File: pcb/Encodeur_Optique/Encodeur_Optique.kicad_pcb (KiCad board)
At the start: 2 copper layers, 20 x 28.5 mm, 10 parts, among them J1 Conn_01x04, U1 GP1A52LRJ00F, U2 74LVC1G17

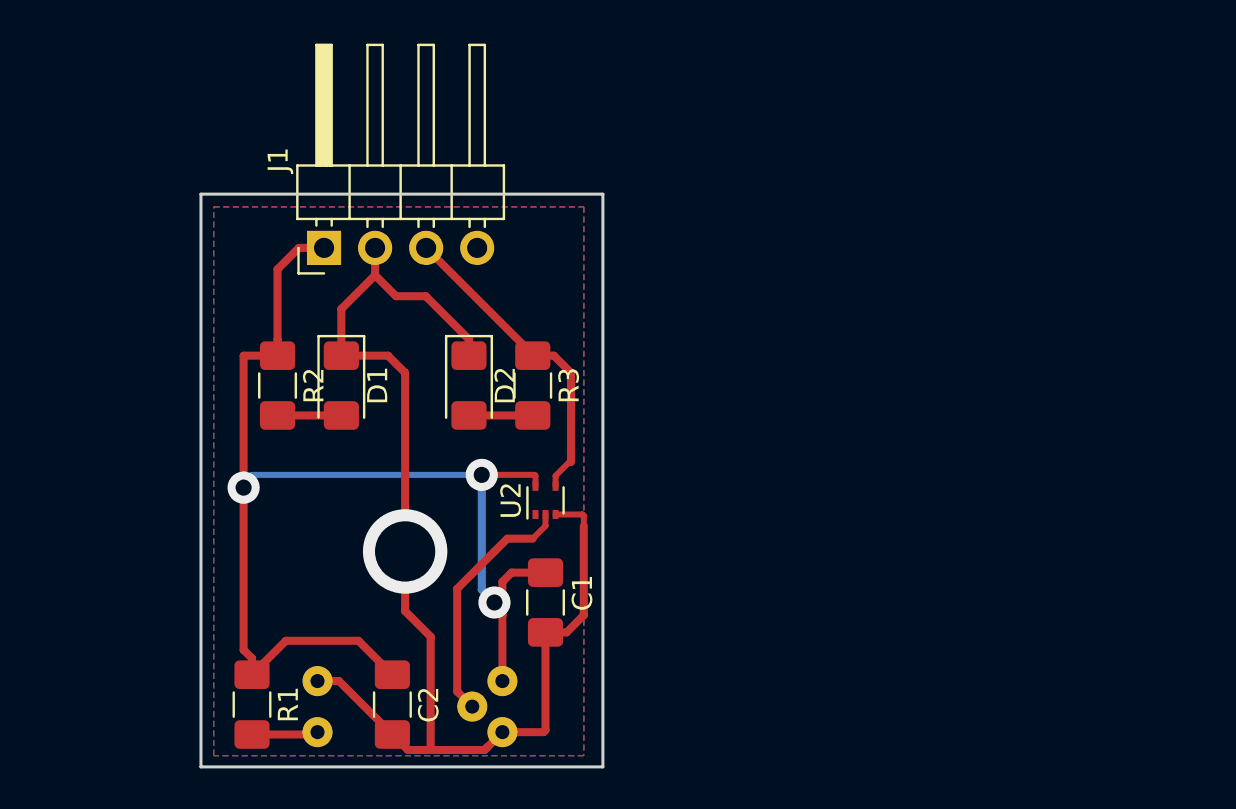
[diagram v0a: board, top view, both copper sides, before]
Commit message: Encoder OK, Camera OK
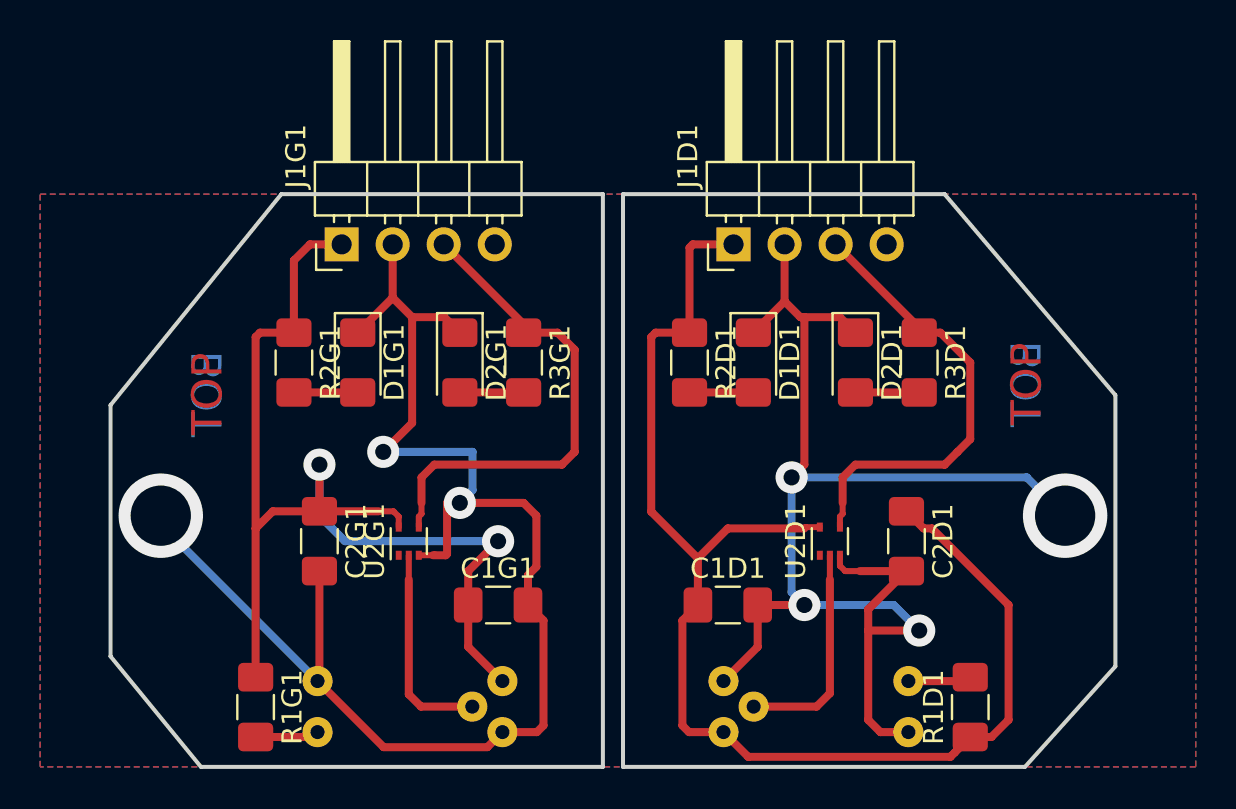
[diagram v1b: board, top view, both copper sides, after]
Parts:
- removed C1, C2: 100nF, Capacitor_SMD:C_1206_3216Metric_Pad1.42x1.75mm_HandSolder
- removed D1: Led Verte, LED_SMD:LED_1206_3216Metric_Pad1.42x1.75mm_HandSolder
- removed D2: Led Rouge, LED_SMD:LED_1206_3216Metric_Pad1.42x1.75mm_HandSolder
- removed J1: Conn_01x04, Connector_PinHeader_2.54mm:PinHeader_1x04_P2.54mm_Horizontal
- removed R1, R2, R3: R, Resistor_SMD:R_1206_3216Metric_Pad1.42x1.75mm_HandSolder
- removed U1: GP1A52LRJ00F, Insa:GP1A52LRJ00F
- removed U2: 74LVC1G17, Package_TO_SOT_SMD:SOT-553
- added C1D1: 100nF, Capacitor_SMD:C_1206_3216Metric_Pad1.42x1.75mm_HandSolder, F.Cu at (131.2, 84.4)
- added C1G1: 100nF, Capacitor_SMD:C_1206_3216Metric_Pad1.42x1.75mm_HandSolder, F.Cu at (119.8, 84.4)
- added C2D1: 100nF, Capacitor_SMD:C_1206_3216Metric_Pad1.42x1.75mm_HandSolder, F.Cu at (140.1, 81.3)
- added C2G1: 100nF, Capacitor_SMD:C_1206_3216Metric_Pad1.42x1.75mm_HandSolder, F.Cu at (110.9, 81.3)
- added D1D1: Led Verte, LED_SMD:LED_1206_3216Metric_Pad1.42x1.75mm_HandSolder, F.Cu at (132.5, 72.4)
- added D1G1: Led Verte, LED_SMD:LED_1206_3216Metric_Pad1.42x1.75mm_HandSolder, F.Cu at (112.8, 72.4)
- added D2D1: Led Rouge, LED_SMD:LED_1206_3216Metric_Pad1.42x1.75mm_HandSolder, F.Cu at (137.6, 72.4)
- added D2G1: Led Rouge, LED_SMD:LED_1206_3216Metric_Pad1.42x1.75mm_HandSolder, F.Cu at (117.9, 72.4)
- added J1D1: Conn_01x04, Connector_PinHeader_2.54mm:PinHeader_1x04_P2.54mm_Horizontal, F.Cu at (131.5, 66.5)
- added J1G1: Conn_01x04, Connector_PinHeader_2.54mm:PinHeader_1x04_P2.54mm_Horizontal, F.Cu at (112.0, 66.5)
- added R1D1: R, Resistor_SMD:R_1206_3216Metric_Pad1.42x1.75mm_HandSolder, F.Cu at (143.3, 89.5)
- added R1G1: R, Resistor_SMD:R_1206_3216Metric_Pad1.42x1.75mm_HandSolder, F.Cu at (107.7, 89.5)
- added R2D1: R, Resistor_SMD:R_1206_3216Metric_Pad1.42x1.75mm_HandSolder, F.Cu at (129.3, 72.4)
- added R2G1: R, Resistor_SMD:R_1206_3216Metric_Pad1.42x1.75mm_HandSolder, F.Cu at (109.6, 72.4)
- added R3D1: R, Resistor_SMD:R_1206_3216Metric_Pad1.42x1.75mm_HandSolder, F.Cu at (140.7, 72.4)
- added R3G1: R, Resistor_SMD:R_1206_3216Metric_Pad1.42x1.75mm_HandSolder, F.Cu at (121.1, 72.4)
- added U1D1: GP1A52LRJ00F, Insa:GP1A52LRJ00F, B.Cu at (136.0, 89.5)
- added U1G1: GP1A52LRJ00F, Insa:GP1A52LRJ00F, B.Cu at (115.0, 89.5)
- added U2D1: 74LVC1G17, Package_TO_SOT_SMD:SOT-553, F.Cu at (136.3, 81.3)
- added U2G1: 74LVC1G17, Package_TO_SOT_SMD:SOT-553, F.Cu at (115.3, 81.3)
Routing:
- net GND: track 62.4 -> 141.9 mm, vias 1 -> 7
- net VCC: track 63.6 -> 122.1 mm, vias 3 -> 2
- net /OUT_G: track 0.00 -> 24.7 mm
- net /OUT_D: track 0.00 -> 22.8 mm
- net /OUT: track 15.8 -> 0.00 mm
- net Net-(U1-Pad4): track 12.4 -> 0.00 mm
- net Net-(U1D1-Pad4): track 0.00 -> 10.9 mm
- net Net-(U1G1-Pad4): track 0.00 -> 10.3 mm
- net Net-(R1-Pad2): track 3.31 -> 0.00 mm
- net Net-(R1G1-Pad2): track 0.00 -> 3.18 mm
- net Net-(D2G1-Pad2): track 0.00 -> 3.18 mm
- net Net-(D2D1-Pad2): track 0.00 -> 3.18 mm
- net Net-(D2-Pad2): track 3.18 -> 0.00 mm
- net Net-(D1D1-Pad2): track 0.00 -> 3.18 mm
- net Net-(D1G1-Pad2): track 0.00 -> 3.17 mm
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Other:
- board size 20 x 28.5 mm -> 50 x 28.5 mm
- board text added: "BOT"
- board text added: "TOP"
